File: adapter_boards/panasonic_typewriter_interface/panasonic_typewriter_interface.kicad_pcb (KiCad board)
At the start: 2 copper layers, 37.3 x 45.7 mm, 27 parts, among them J1 KMDGX-8S-AS, J2 Conn_02x03_Odd_Even, J3 Conn_01x06_MountingPin, J4 Conn_01x06_MountingPin, J5 Conn_01x04_MountingPin, SW1 SW_SPDT, SW2 SW_Push

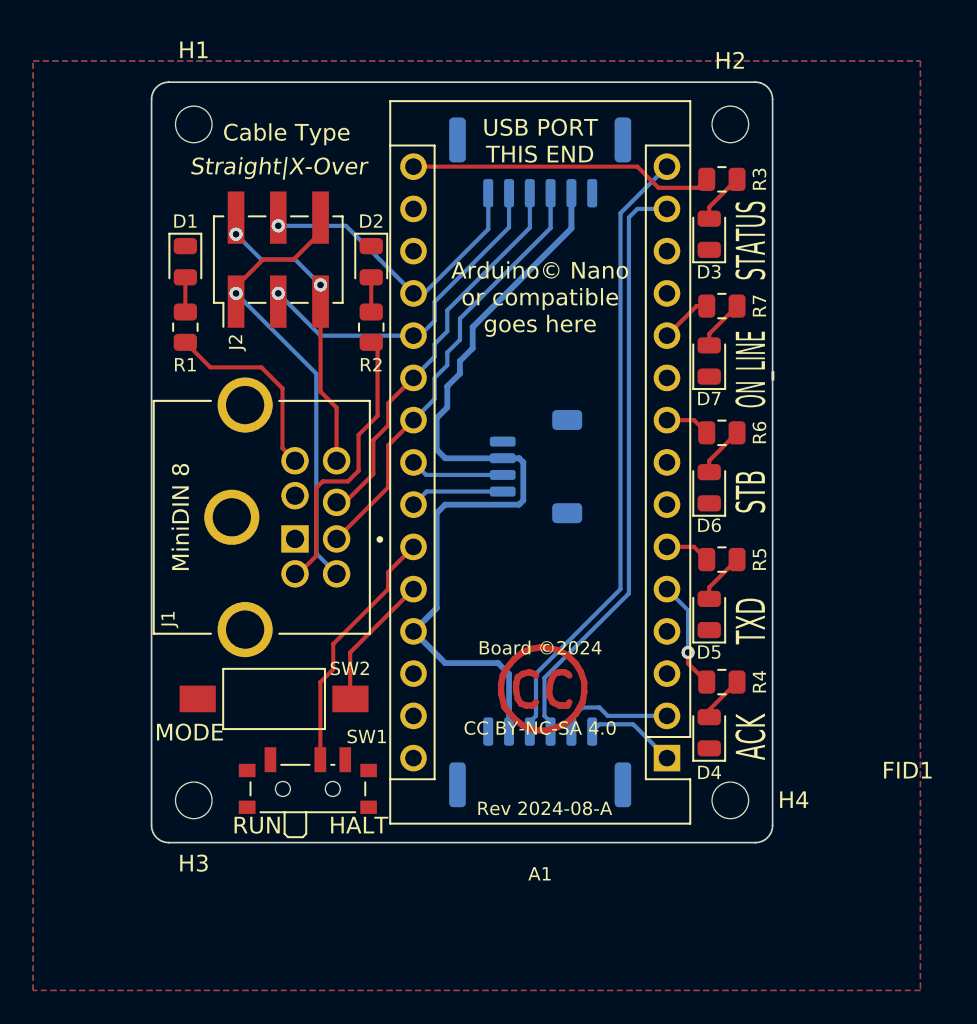
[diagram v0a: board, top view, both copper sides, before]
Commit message: Adjust the mount spacing for more round numbers
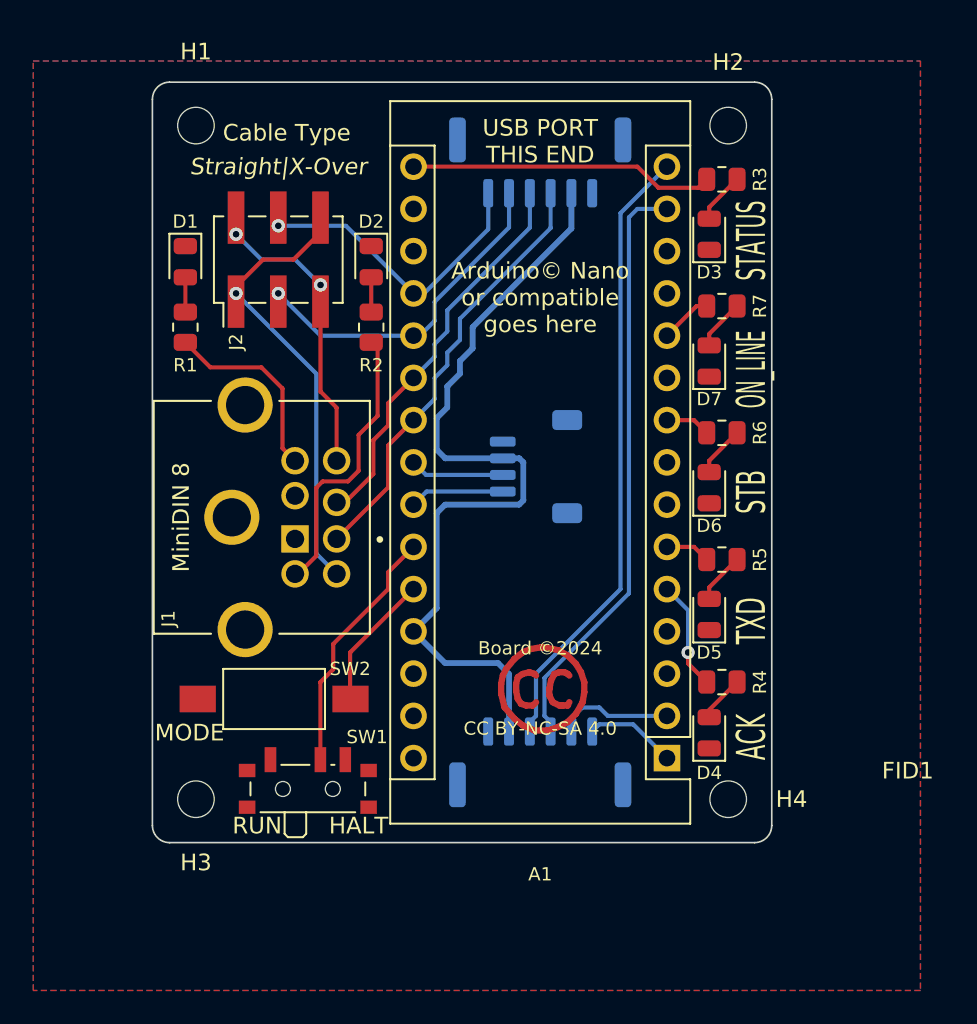
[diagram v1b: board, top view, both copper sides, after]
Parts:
- moved H2 0.15 mm to (156.1, 68.7)
- moved H4 0.15 mm to (156.1, 109.2)
- moved H1 0.15 mm to (124.1, 68.7)
- moved H3 0.15 mm to (124.1, 109.2)
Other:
- board size 37.3 x 45.7 mm -> 37.2 x 45.7 mm
- board text added: "1"
- board text added: "2"
- board text added: "3"
- board text added: "4"
- board text added: "5"
- board text added: "6"
- board text added: "7"
- board text added: "8"
- board text added: "I routed +5V like this just to avoid using a 2 more vias!"
- board text added: "Mounting Holes: Size: M2 Spacing: 40.5mm x 32mm"
- board text removed: "I routed +5V like this just to avoid using a few more vias!"
- board text removed: "Mounting Holes: Size: M2 Spacing: 40.6mm x 32.6mm"

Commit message: isquare up the mounting holes even more; label the connectors better
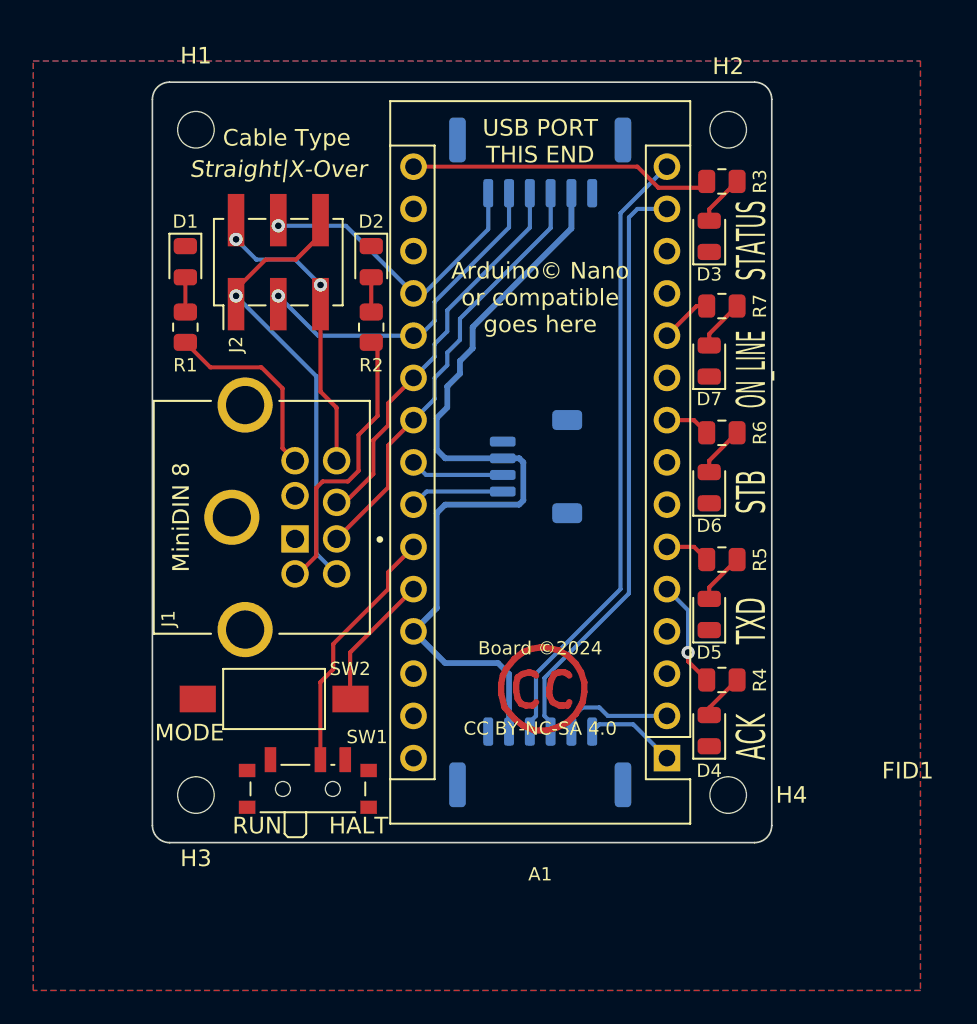
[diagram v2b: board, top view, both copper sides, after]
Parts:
- moved H1 0.25 mm to (124.1, 68.9)
- moved H2 0.25 mm to (156.1, 68.9)
- moved H3 0.25 mm to (124.1, 108.9)
- moved H4 0.25 mm to (156.1, 108.9)
- moved J2 0.15 mm to (129.0, 76.9)
- moved D3 0.13 mm to (154.9, 75.3)
- moved D4 0.13 mm to (154.9, 105.0)
- moved R4 0.13 mm to (155.7, 102.0)
- moved R3 0.13 mm to (155.7, 72.0)
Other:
- board text added: "JST GH"
- board text added: "JST SH"
- board text added: "Mounting Holes: Size: M2 Spacing: 40mm x 32mm"
- board text removed: "Mounting Holes: Size: M2 Spacing: 40.5mm x 32mm"

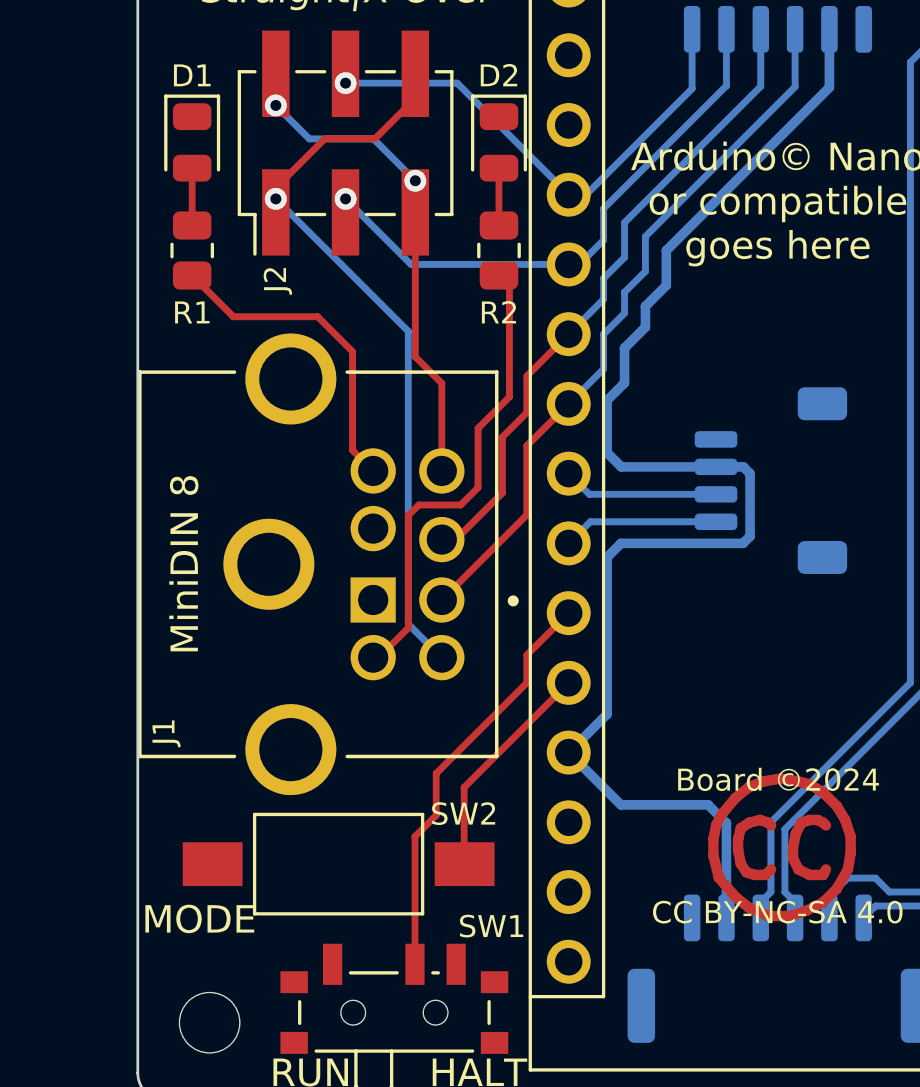
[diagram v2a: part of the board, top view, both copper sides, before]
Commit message: Add fuse to main 5v rail; label unused IO pins; minor silkscreen mods
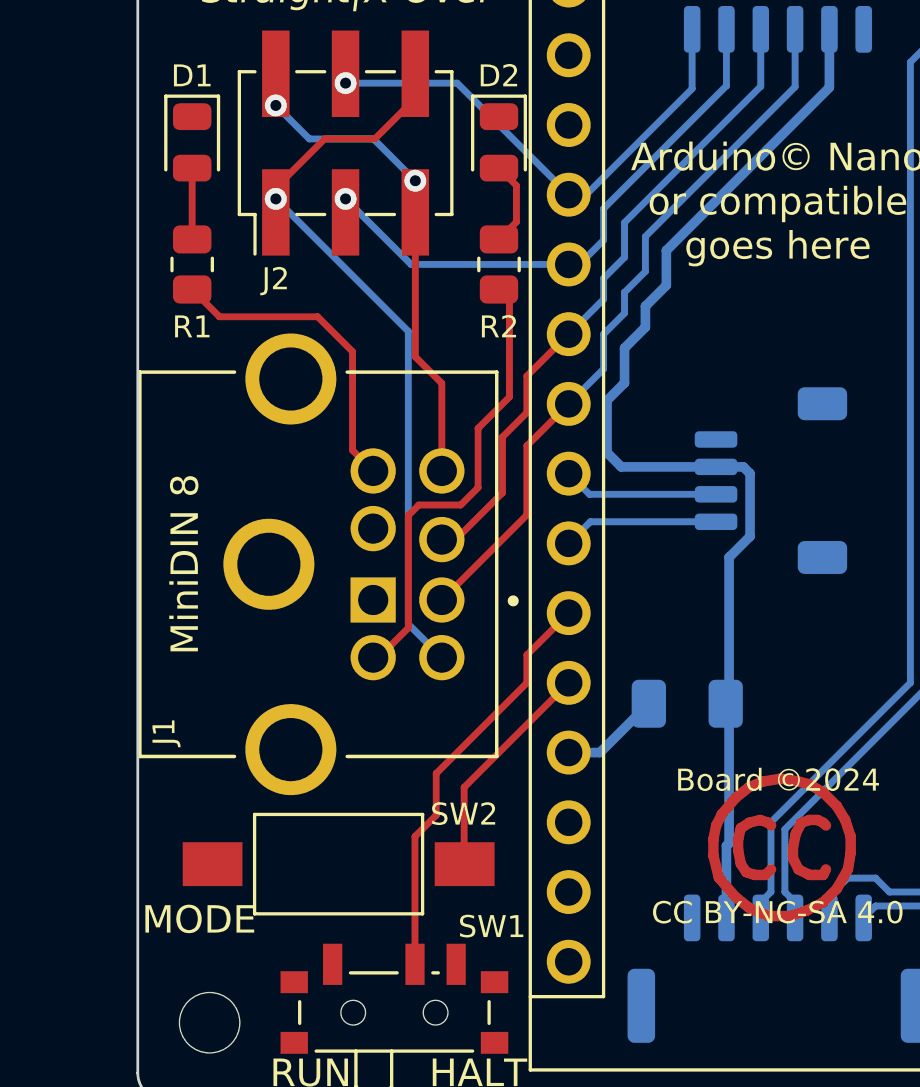
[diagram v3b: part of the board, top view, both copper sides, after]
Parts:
- added F1: Polyfuse, Fuse:Fuse_1206_3216Metric, B.Cu at (141.5, 97.3)
- moved R1 0.51 mm to (123.4, 81.3)
- moved R2 0.51 mm to (134.6, 81.3)
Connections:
- A1 pad 27: +5V -> Net-(A1-Pad27)
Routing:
- net +5V: track 50.1 -> 40.9 mm
- net Net-(A1-Pad27): track 0.00 -> 3.65 mm
- net Net-(D2-Pad2): track 2.09 -> 3.12 mm
- net Net-(D1-Pad2): track 2.09 -> 2.60 mm
- net +12V_CROSS: track 17.1 -> 16.6 mm
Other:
- board text added: "3V3"
- board text added: "AREF"
- board text added: "Cable Type: J2 Move BOTH jumpers on J2 to either STRAIGHT or X-OVER. If connecting KX-R, LEDs D1/D2 show current cable type but jumpers must still be moved to side closest to lit LED."
- board text added: "D10"
- board text added: "D4"
- board text added: "D5"
- board text added: "D7"
- board text added: "D9"
- board text added: "I routed +5V like this just to avoid 2 extra vias!"
- board text added: "Mounting Holes: Size: M2 Spacing: 40 x 32 mm"
- board text added: "RESET"
- board text added: "Rev 2024-10-A"
- board text added: "Stemma QT compatible"
- board text added: "VIN"
- board text removed: "Adafruit© Stemma QT compatible"
- board text removed: "Cable Type (J2): Move both jumpers on J2 to either STRAIGHT or X-OVER. If connecting KX-R, LEDs D1/D2 show current cable type but jumpers must still be moved to side closest to lit LED."
- board text removed: "I routed +5V like this just to avoid using a 2 more vias!"
- board text removed: "Mounting Holes: Size: M2 Spacing: 40mm x 32mm"
- board text removed: "Rev 2024-08-A"

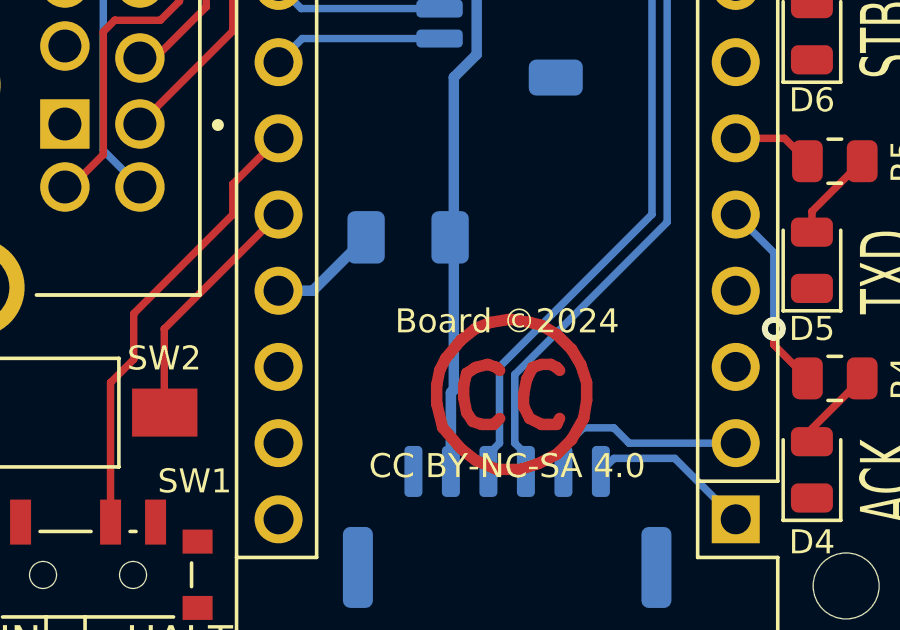
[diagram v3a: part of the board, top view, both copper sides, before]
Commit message: couple more labels
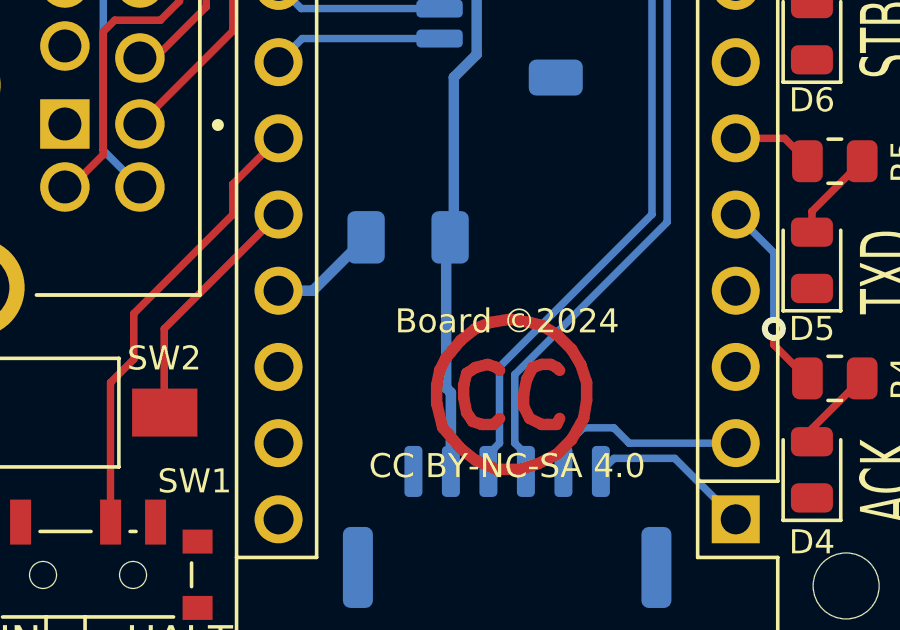
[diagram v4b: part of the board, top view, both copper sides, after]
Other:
- board text added: "5V"
- board text added: "~{RESET}"
- board text added: "~{R}"
- board text removed: "RESET"
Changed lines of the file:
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@@
     (effects (font (size 0.8 0.8) (thickness 0.15) italic) (justify mirror))
   )
-  (gr_text "Mounting Holes:\n\nSize: M2\nSpacing:\n  40 x 32 mm" (at 132.588 104.14) (layer "B.SilkS")
+  (gr_text "Mounting Holes:\n\nSize: M2\nSpacing:\n  40 x 32 mm" (at 132.334 103.886) (layer "B.SilkS")
     (effects (font (size 0.8 0.8) (thickness 0.15)) (justify left mirror))
   )
@@
     (effects (font (size 0.8 0.8) (thickness 0.15)) (justify right mirror))
   )
+  (gr_text "5V" (at 136.144 99.06 45) (layer "B.SilkS")
+    (effects (font (size 0.8 0.8) (thickness 0.15)) (justify left mirror))
+  )
   (gr_text "~{STB}" (at 144.018 74.168 270) (layer "B.SilkS")
     (effects (font (size 0.8 0.8) (thickness 0.15)) (justify right mirror))
@@
     (effects (font (size 0.8 0.8) (thickness 0.15)) (justify left mirror))
   )
-  (gr_text "AREF" (at 138.176 76.2 315) (layer "B.SilkS")
+  (gr_text "AREF" (at 137.922 76.708 315) (layer "B.SilkS")
     (effects (font (size 0.8 0.8) (thickness 0.15)) (justify right mirror))
   )
@@
     (effects (font (size 0.8 0.8) (thickness 0.15)) (justify left mirror))
   )
-  (gr_text "3V3" (at 138.176 73.66 315) (layer "B.SilkS")
+  (gr_text "3V3" (at 137.922 74.168 315) (layer "B.SilkS")
     (effects (font (size 0.8 0.8) (thickness 0.15)) (justify right mirror))
   )
@@
     (effects (font (size 0.8 0.8) (thickness 0.15)) (justify mirror))
   )
+  (gr_text "~{R}" (at 151.384 101.6 45) (layer "B.SilkS")
+    (effects (font (size 0.8 0.8) (thickness 0.15)) (justify left mirror))
+  )
   (gr_text "JST GH" (at 144.78 108.585) (layer "B.SilkS")
     (effects (font (size 0.8 0.8) (thickness 0.15) italic) (justify mirror))
@@
     (effects (font (size 0.8 0.8) (thickness 0.15)) (justify left mirror))
   )
-  (gr_text "RESET" (at 136.144 101.6 45) (layer "B.SilkS")
+  (gr_text "~{RESET}" (at 136.144 101.6 45) (layer "B.SilkS")
     (effects (font (size 0.8 0.8) (thickness 0.15)) (justify left mirror))
   )
@@
   (segment (start 149.606 96.52) (end 149.606 73.914) (width 0.25) (layer "B.Cu") (net 31))
   (segment (start 144.272 104.967) (end 144.272 104.394) (width 0.25) (layer "B.Cu") (net 31))
-  (segment (start 142.905 102.4555) (end 143.002 102.3585) (width 0.35) (layer "B.Cu") (net 35))
+  (segment (start 142.905 105.084) (end 142.905 102.4555) (width 0.35) (layer "B.Cu") (net 35))
   (segment (start 140.716 82.042) (end 140.716 80.772) (width 0.35) (layer "B.Cu") (net 35))
-  (segment (start 143.002 97.406) (end 142.878 97.282) (width 0.35) (layer "B.Cu") (net 35))
   (segment (start 138.557 86.233) (end 139.192 85.598) (width 0.35) (layer "B.Cu") (net 35))
   (segment (start 139.192 85.598) (end 139.192 84.328) (width 0.35) (layer "B.Cu") (net 35))
+  (segment (start 142.905 102.4555) (end 142.748 102.2985) (width 0.35) (layer "B.Cu") (net 35))
   (segment (start 143.764 91.186) (end 143.764 88.9) (width 0.35) (layer "B.Cu") (net 35))
   (segment (start 143.002 97.158) (end 143.002 91.948) (width 0.35) (layer "B.Cu") (net 35))
@@
   (segment (start 139.954 83.566) (end 139.954 82.804) (width 0.35) (layer "B.Cu") (net 35))
   (segment (start 138.557 88.138) (end 138.557 86.233) (width 0.35) (layer "B.Cu") (net 35))
-  (segment (start 142.905 105.084) (end 142.905 102.4555) (width 0.35) (layer "B.Cu") (net 35))
   (segment (start 142.526 88.654) (end 139.073 88.654) (width 0.35) (layer "B.Cu") (net 35))
   (segment (start 146.655 74.833) (end 146.655 72.716) (width 0.35) (layer "B.Cu") (net 35))
   (segment (start 139.954 82.804) (end 140.716 82.042) (width 0.35) (layer "B.Cu") (net 35))
   (segment (start 143.002 91.948) (end 143.764 91.186) (width 0.35) (layer "B.Cu") (net 35))
-  (segment (start 143.002 102.3585) (end 143.002 97.406) (width 0.35) (layer "B.Cu") (net 35))
+  (segment (start 142.748 102.2985) (end 142.748 97.412) (width 0.35) (layer "B.Cu") (net 35))
+  (segment (start 142.748 97.412) (end 142.878 97.282) (width 0.35) (layer "B.Cu") (net 35))
   (segment (start 142.878 97.282) (end 143.002 97.158) (width 0.35) (layer "B.Cu") (net 35))
   (segment (start 139.073 88.654) (end 138.557 88.138) (width 0.35) (layer "B.Cu") (net 35))

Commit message: Nudge resistors around for better ground path
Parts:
- moved R4 0.38 mm to (155.7, 101.6)
- moved D5 0.36 mm to (155.2, 97.8)
- moved D4 0.28 mm to (155.2, 104.9)
- moved R5 0.25 mm to (155.7, 94.5)
- moved D3 0.25 mm to (155.2, 75.3)
- moved D6 0.25 mm to (155.2, 90.4)
- moved D7 0.25 mm to (155.2, 82.8)
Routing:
- net ACK_LED: track 6.45 -> 8.22 mm, vias 1 -> 0
- net ~{ACK}: track 26.1 -> 26.6 mm
- net GND: track 0.37 -> 0.00 mm, vias 0 -> 1
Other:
- board text added: "I routed +5V like this just to avoid extra vias!"
- board text removed: "I routed +5V like this just to avoid 2 extra vias!"
